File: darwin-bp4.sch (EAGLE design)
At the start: 11 parts

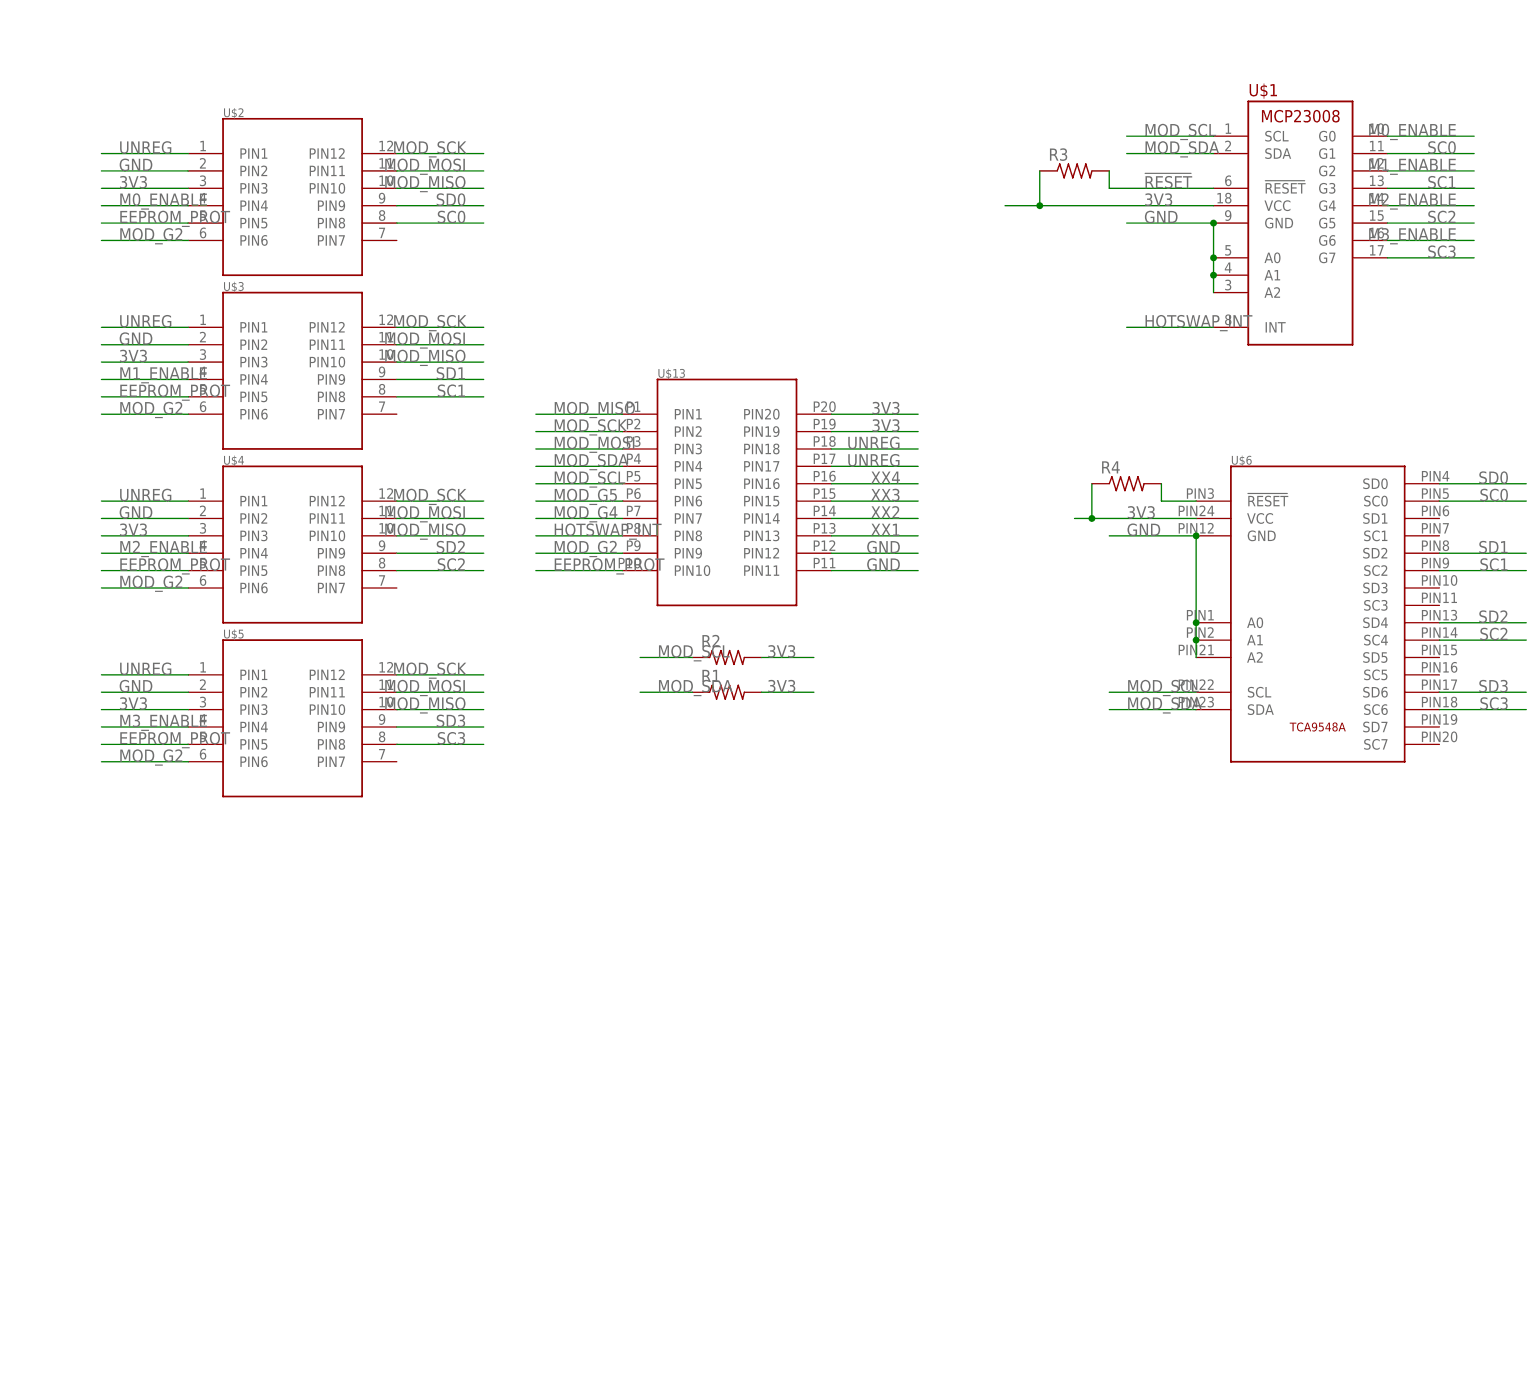
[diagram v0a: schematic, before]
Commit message: Added LEDs and decoupling.
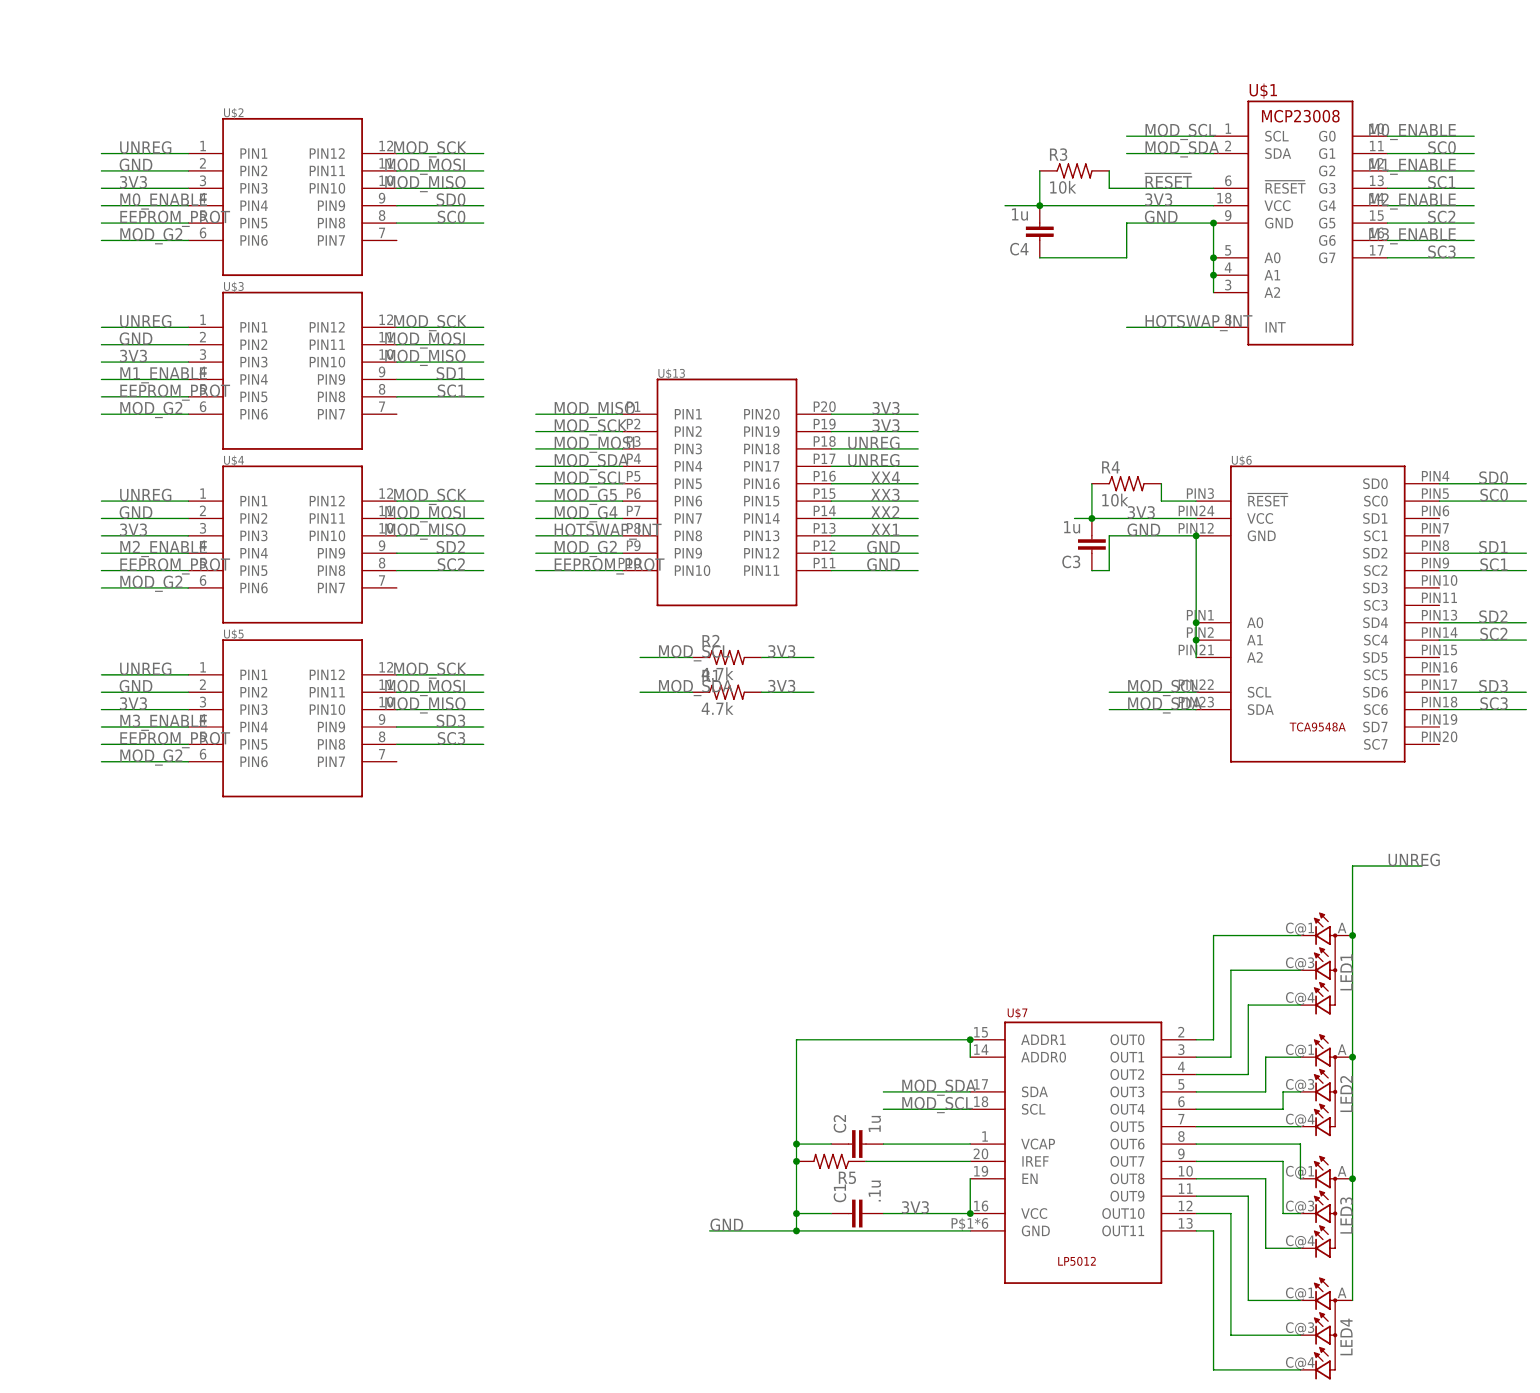
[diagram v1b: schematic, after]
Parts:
- added C1: .1u, rcl:C-EUC0603K
- added C2, C3, C4: 1u, rcl:C-EUC0603K
- added LED1, LED2, LED3, LED4: (no value), led:TOPLED-3P-LCC-4
- added R5: (no value), rcl:R-US_R0603
- added U$7: LP5012, Conservify:LP5012
- R1, R2: value (none) -> 4.7k
- R3, R4: value (none) -> 10k
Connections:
- new net N$1: LED1.CRED, U$7.OUT0
- new net N$11: LED3.CGREEN, U$7.OUT8
- new net N$12: LED4.CRED, U$7.OUT9
- new net N$13: LED4.CBLUE, U$7.OUT10
- new net N$14: LED4.CGREEN, U$7.OUT11
- new net N$20: C2.2, U$7.VCAP
- new net N$21: R5.1, U$7.IREF
- new net N$3: LED1.CBLUE, U$7.OUT1
- new net N$4: LED1.CGREEN, U$7.OUT2
- new net N$5: LED2.CRED, U$7.OUT3
- new net N$6: LED2.CBLUE, U$7.OUT4
- new net N$7: LED2.CGREEN, U$7.OUT5
- new net N$8: LED3.CRED, U$7.OUT6
- new net N$9: LED3.CBLUE, U$7.OUT7
- net 3V3: now also C1.2, C3.2, C4.2, U$7.EN, U$7.VCC
- net GND: now also C1.1, C2.1, C3.1, C4.1, R5.2, U$7.ADDR0, U$7.ADDR1, U$7.GND
- net MOD_SCL: now also U$7.SCL
- net MOD_SDA: now also U$7.SDA
- net UNREG: now also LED1.A2, LED2.A2, LED3.A2, LED4.A2

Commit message: Cleanup.
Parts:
- removed U$1: MCP23008, Conservify:MCP23008
- removed U$13: M55-6102042R7102(M), Conservify:M55-6102042R7102(M)
- removed U$6: TCA9548A, Conservify:TCA9548A
- removed U$7: LP5012, Conservify:LP5012
- added MEZZ-TO-RADIO: M55-6102042R7102(M), Conservify:M55-6102042R7102(M)
- added U1: MCP23008, Conservify:MCP23008
- added U2: TCA9548A, Conservify:TCA9548A
- added U3: LP5012, Conservify:LP5012
- C3, C4: value 1u -> .1uf
- renumbered U$2 to SLOT1, U$3 to SLOT2, U$4 to SLOT3, U$5 to SLOT4
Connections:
- net !RESET: now also U1.!RESET; no longer U$1.!RESET
- net 3V3: now also MEZZ-TO-RADIO.PIN19, MEZZ-TO-RADIO.PIN20, U1.VCC, U2.VCC, U3.EN, U3.VCC; no longer U$1.VCC, U$13.PIN19, U$13.PIN20, U$6.VCC, U$7.EN, U$7.VCC
- net EEPROM_PROT: now also MEZZ-TO-RADIO.PIN10; no longer U$13.PIN10
- net GND: now also MEZZ-TO-RADIO.PIN11, MEZZ-TO-RADIO.PIN12, U1.A0, U1.A1, U1.A2, U1.GND, U2.A0, U2.A1, U2.A2, U2.GND, U3.ADDR0, U3.ADDR1, U3.GND; no longer U$1.A0, U$1.A1, U$1.A2, U$1.GND, U$13.PIN11, U$13.PIN12, U$6.A0, U$6.A1, U$6.A2, U$6.GND, U$7.ADDR0, U$7.ADDR1, U$7.GND
- net HOTSWAP_INT: now also MEZZ-TO-RADIO.PIN8, U1.INT; no longer U$1.INT, U$13.PIN8
- net M0_ENABLE: now also U1.G0; no longer U$1.G0
- net M1_ENABLE: now also U1.G2; no longer U$1.G2
- net M2_ENABLE: now also U1.G4; no longer U$1.G4
- net M3_ENABLE: now also U1.G6; no longer U$1.G6
- net MOD_G2: now also MEZZ-TO-RADIO.PIN9; no longer U$13.PIN9
- net MOD_G4: now also MEZZ-TO-RADIO.PIN7; no longer U$13.PIN7
- net MOD_G5: now also MEZZ-TO-RADIO.PIN6; no longer U$13.PIN6
- net MOD_MISO: now also MEZZ-TO-RADIO.PIN1; no longer U$13.PIN1
- net MOD_MOSI: now also MEZZ-TO-RADIO.PIN3; no longer U$13.PIN3
- net MOD_SCK: now also MEZZ-TO-RADIO.PIN2; no longer U$13.PIN2
- net MOD_SCL: now also MEZZ-TO-RADIO.PIN5, U1.SCL, U2.SCL, U3.SCL; no longer U$1.SCL, U$13.PIN5, U$6.SCL, U$7.SCL
- net MOD_SDA: now also MEZZ-TO-RADIO.PIN4, U1.SDA, U2.SDA, U3.SDA; no longer U$1.SDA, U$13.PIN4, U$6.SDA, U$7.SDA
- net N$1: now also U3.OUT0; no longer U$7.OUT0
- net N$11: now also U3.OUT8; no longer U$7.OUT8
- net N$12: now also U3.OUT9; no longer U$7.OUT9
- net N$13: now also U3.OUT10; no longer U$7.OUT10
- net N$14: now also U3.OUT11; no longer U$7.OUT11
- net N$2: now also U2.!RESET; no longer U$6.!RESET
- net N$20: now also U3.VCAP; no longer U$7.VCAP
- net N$21: now also U3.IREF; no longer U$7.IREF
- net N$3: now also U3.OUT1; no longer U$7.OUT1
- net N$4: now also U3.OUT2; no longer U$7.OUT2
- net N$5: now also U3.OUT3; no longer U$7.OUT3
- net N$6: now also U3.OUT4; no longer U$7.OUT4
- net N$7: now also U3.OUT5; no longer U$7.OUT5
- net N$8: now also U3.OUT6; no longer U$7.OUT6
- net N$9: now also U3.OUT7; no longer U$7.OUT7
- net SC0: now also U1.G1, U2.SC0; no longer U$1.G1, U$6.SC0
- net SC1: now also U1.G3, U2.SC2; no longer U$1.G3, U$6.SC2
- net SC2: now also U1.G5, U2.SC4; no longer U$1.G5, U$6.SC4
- net SC3: now also U1.G7, U2.SC6; no longer U$1.G7, U$6.SC6
- net SD0: now also U2.SD0; no longer U$6.SD0
- net SD1: now also U2.SD2; no longer U$6.SD2
- net SD2: now also U2.SD4; no longer U$6.SD4
- net SD3: now also U2.SD6; no longer U$6.SD6
- net UNREG: now also MEZZ-TO-RADIO.PIN17, MEZZ-TO-RADIO.PIN18; no longer U$13.PIN17, U$13.PIN18
- net XX1: now also MEZZ-TO-RADIO.PIN13; no longer U$13.PIN13
- net XX2: now also MEZZ-TO-RADIO.PIN14; no longer U$13.PIN14
- net XX3: now also MEZZ-TO-RADIO.PIN15; no longer U$13.PIN15
- net XX4: now also MEZZ-TO-RADIO.PIN16; no longer U$13.PIN16
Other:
- note added: "CONNECTORS"
- note added: "I2C TERMINATION"
- note added: "IO EXP"
- note added: "LEDS+CONTROLLER"
- note added: "MULTIPLEXER"
- moved on the sheet: C1, C2, C3, C4, LED1, LED2, LED3, LED4, R1, R2, R3, R4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

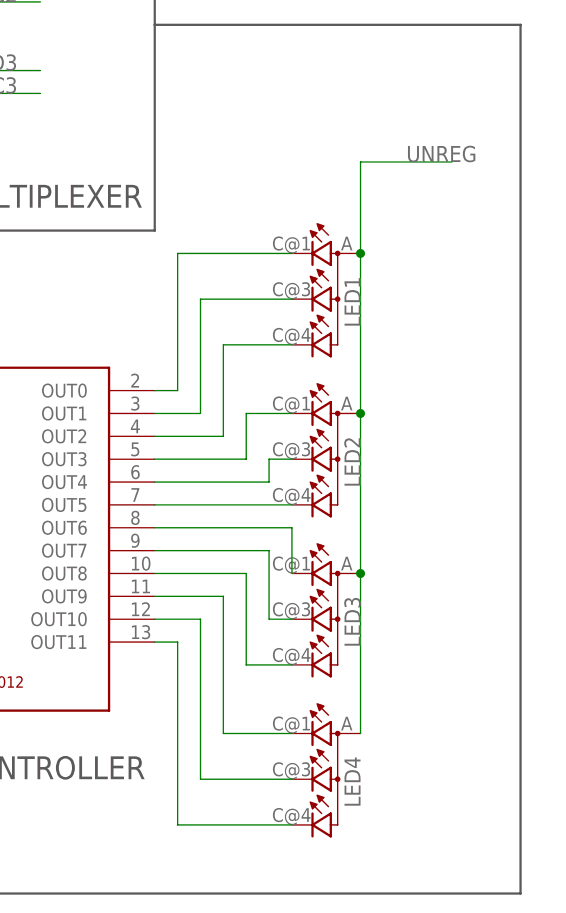
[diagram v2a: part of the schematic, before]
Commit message: Fixed LED footprints and tidied routing.
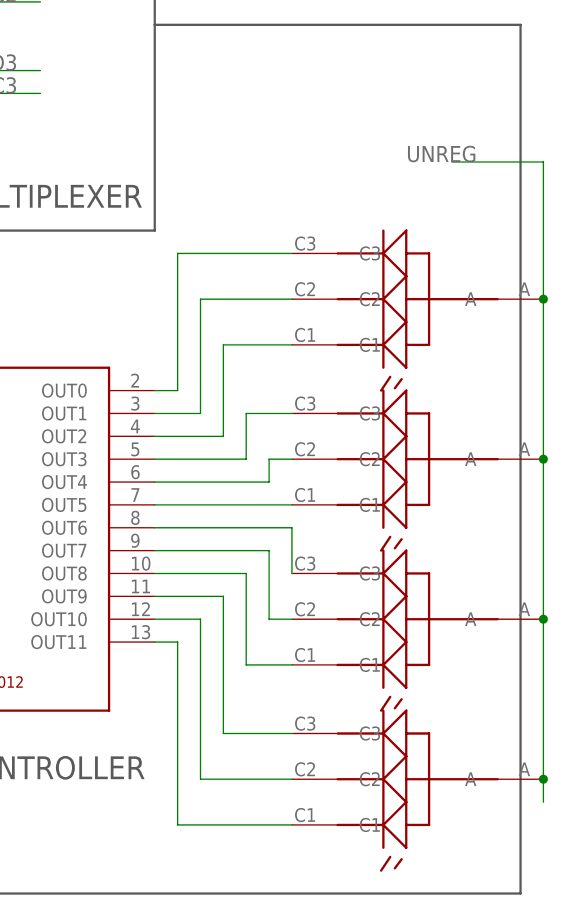
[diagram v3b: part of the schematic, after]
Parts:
- removed LED1, LED2, LED3, LED4: (no value), led:TOPLED-3P-LCC-4
- added U$1, U$2, U$3, U$4: CLMVC-FKC-CGJJM569ABB7A343, Conservify:CLMVC-FKC-CGJJM569ABB7A343
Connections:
- net N$1: now also U$1.C3; no longer LED1.CRED
- net N$11: now also U$3.C1; no longer LED3.CGREEN
- net N$12: now also U$4.C3; no longer LED4.CRED
- net N$13: now also U$4.C2; no longer LED4.CBLUE
- net N$14: now also U$4.C1; no longer LED4.CGREEN
- net N$3: now also U$1.C2; no longer LED1.CBLUE
- net N$4: now also U$1.C1; no longer LED1.CGREEN
- net N$5: now also U$2.C3; no longer LED2.CRED
- net N$6: now also U$2.C2; no longer LED2.CBLUE
- net N$7: now also U$2.C1; no longer LED2.CGREEN
- net N$8: now also U$3.C3; no longer LED3.CRED
- net N$9: now also U$3.C2; no longer LED3.CBLUE
- net UNREG: now also U$1.A, U$2.A, U$3.A, U$4.A; no longer LED1.A2, LED2.A2, LED3.A2, LED4.A2
